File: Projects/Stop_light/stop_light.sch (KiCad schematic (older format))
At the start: 40 parts, among them J1 109159003101916, U1 IS31LT3360, U2 IS31LT3360, U3 IS31LT3360

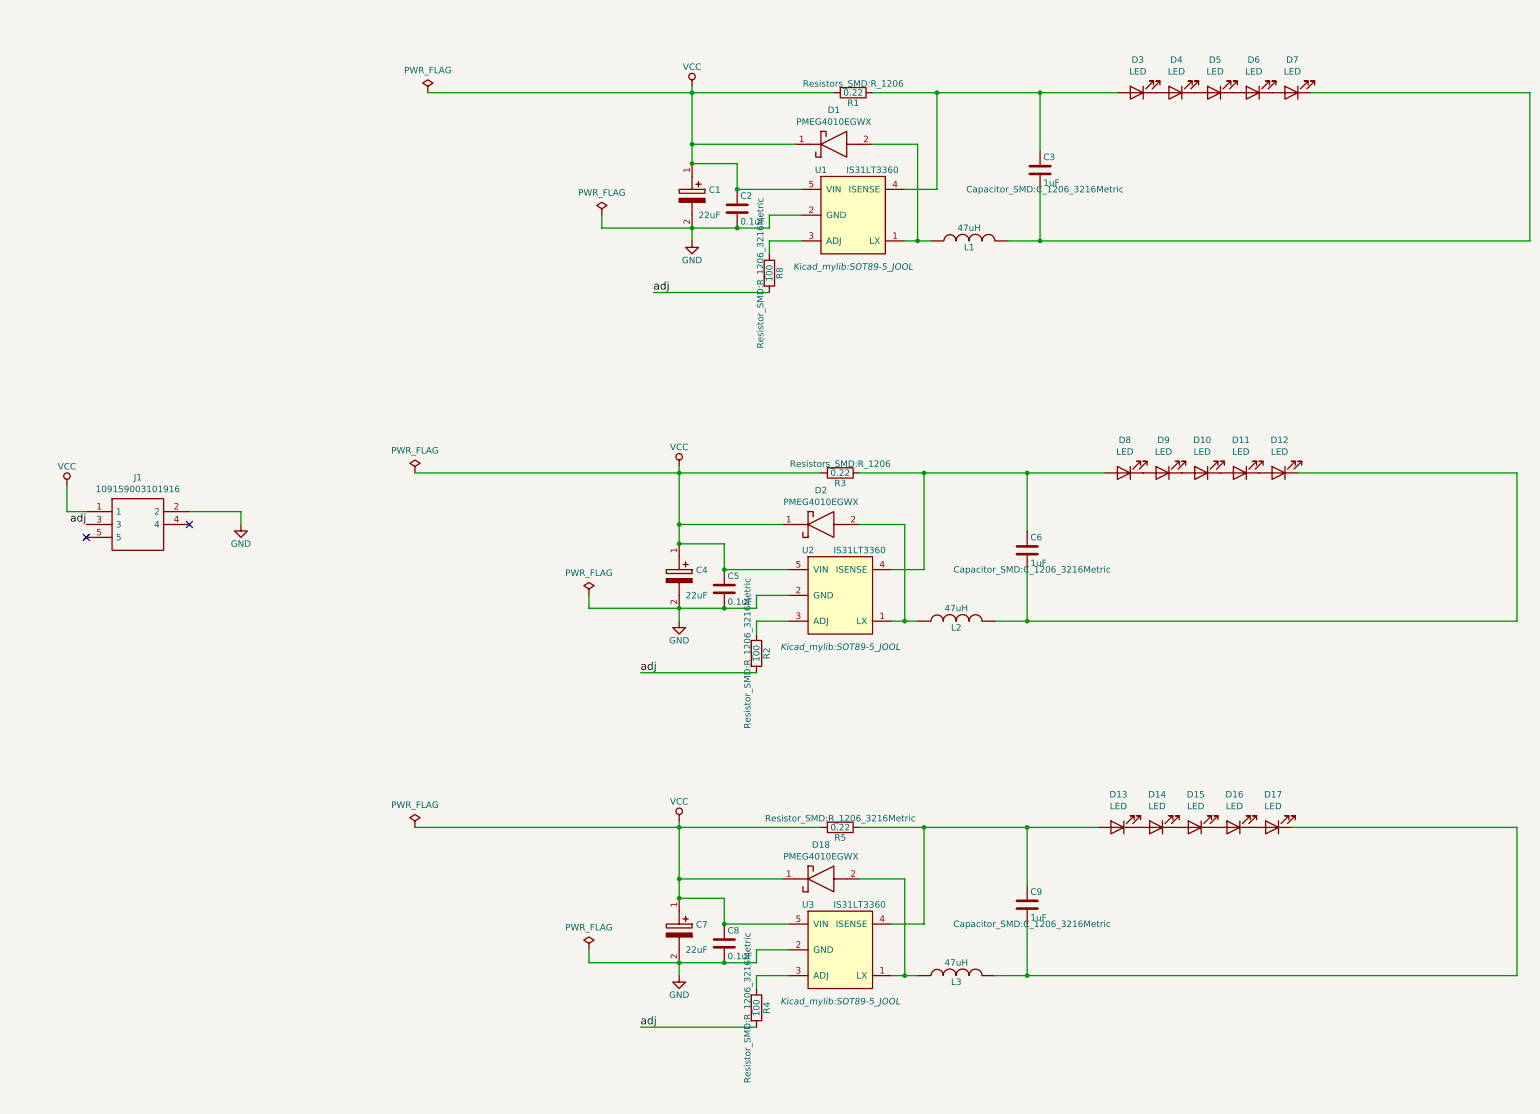
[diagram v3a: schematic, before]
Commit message: stop light updated
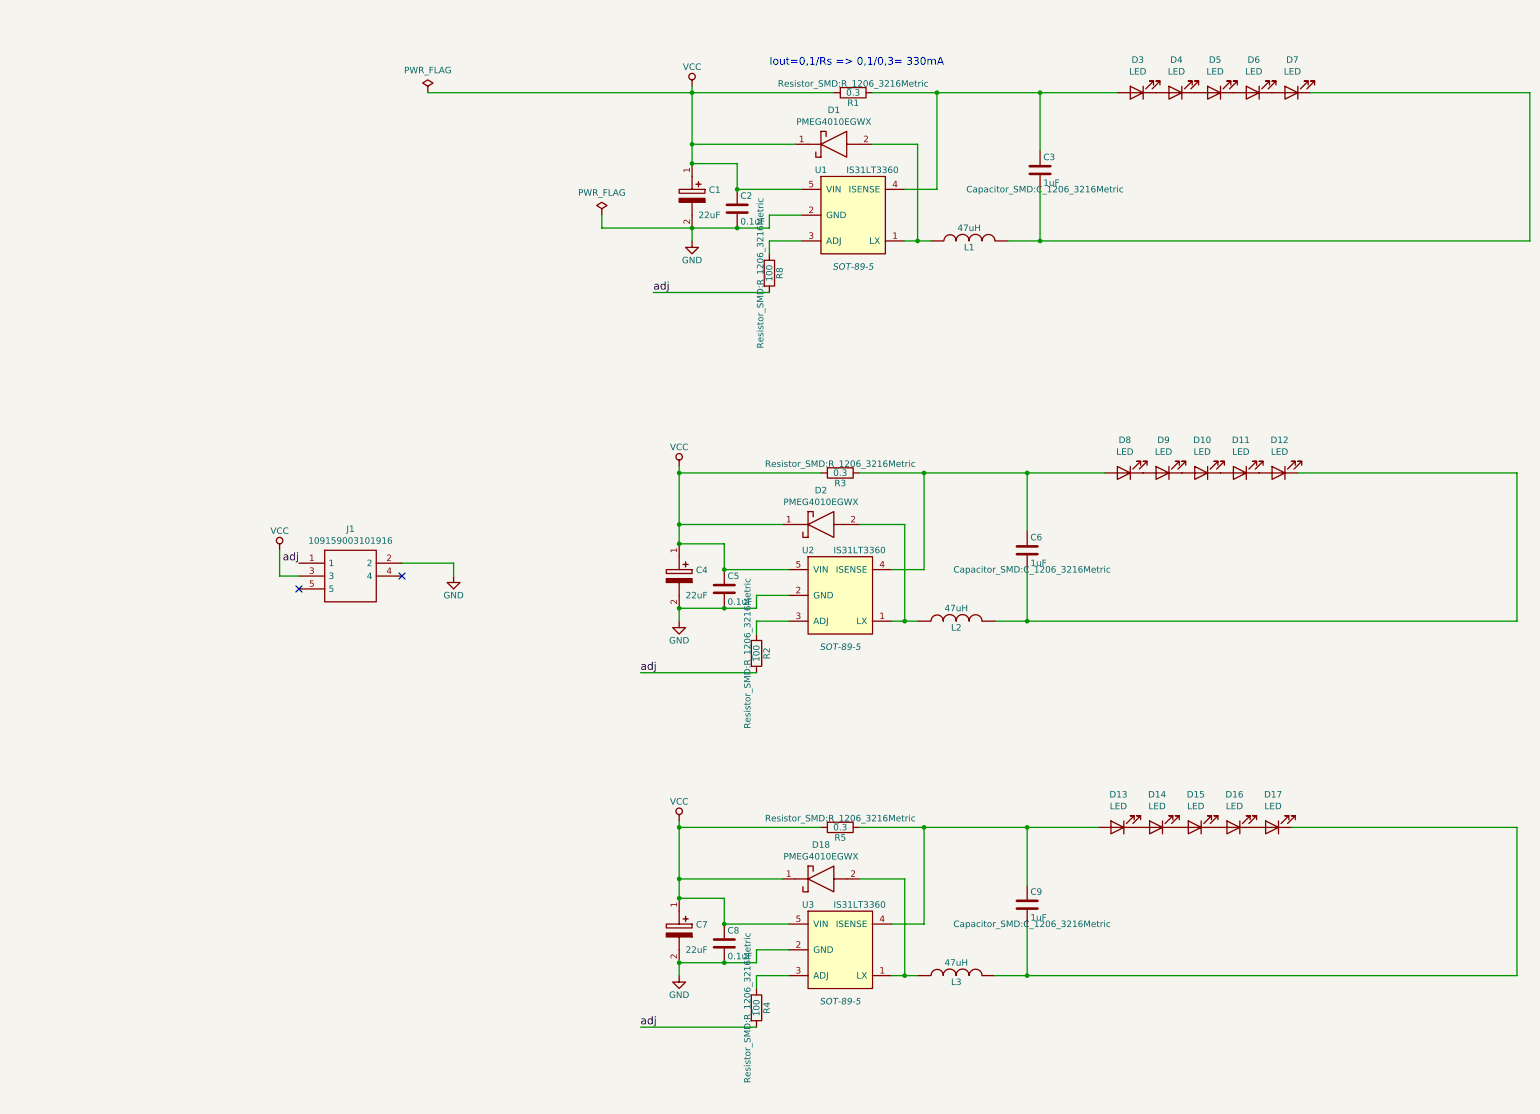
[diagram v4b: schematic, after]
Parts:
- D3: Manufacturer_Part_Number (none) -> DMLQ31.23-HYKY-26-J3T3
- R1, R3: value 0.22 -> 0.3; footprint Resistors_SMD:R_1206 -> Resistor_SMD:R_1206_3216Metric
- R5: value 0.22 -> 0.3
- U1, U2, U3: footprint Kicad_mylib:SOT89-5_JOOL -> SOT-89-5; Manufacturer_Part_Number (none) -> IS31LT3360-SDLS4-TR; Mouser Part Number (none) -> 870-I31LT3360SDLS4TR
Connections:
- net VCC: now also J1.3; no longer J1.1
- net adj: now also J1.1; no longer J1.3
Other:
- note added: "Iout=0,1/Rs => 0,1/0,3= 330mA"
- moved on the sheet: J1
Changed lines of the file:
@@
 F 0 "U1" H 6650 2650 50  0000 C CNN
 F 1 "IS31LT3360" H 7050 2650 50  0000 C CNN
-F 2 "Kicad_mylib:SOT89-5_JOOL" H 6900 1900 50  0000 C CIN
+F 2 "SOT-89-5" H 6900 1900 50  0000 C CIN
 F 3 "www.issi.com/WW/pdf/31LT3360.pdf" H 6950 1800 50  0001 C CNN
+F 4 "IS31LT3360-SDLS4-TR" H 6900 2300 50  0001 C CNN "Manufacturer_Part_Number"
+F 5 "870-I31LT3360SDLS4TR" H 6900 2300 50  0001 C CNN "Mouser Part Number"
 	1    6900 2300
 	1    0    0    -1
@@
 P 6900 1350
 F 0 "R1" V 6980 1350 50  0000 C CNN
-F 1 "0.22" V 6900 1350 50  0000 C CNN
-F 2 "Resistors_SMD:R_1206" V 6830 1350 50  0000 C CNN
+F 1 "0.3" V 6900 1350 50  0000 C CNN
+F 2 "Resistor_SMD:R_1206_3216Metric" V 6830 1350 50  0000 C CNN
 F 3 "" H 6900 1350 50  0000 C CNN
 	1    6900 1350
@@
 F 2 "myKicad_lib:DMLQ31_23" H 9100 1350 50  0001 C CNN
 F 3 "~" H 9100 1350 50  0001 C CNN
+F 4 "DMLQ31.23-HYKY-26-J3T3" H 9100 1350 50  0001 C CNN "Manufacturer_Part_Number"
 	1    9100 1350
 	-1   0    0    1
@@
 F 0 "U2" H 6550 5600 50  0000 C CNN
 F 1 "IS31LT3360" H 6950 5600 50  0000 C CNN
-F 2 "Kicad_mylib:SOT89-5_JOOL" H 6800 4850 50  0000 C CIN
+F 2 "SOT-89-5" H 6800 4850 50  0000 C CIN
 F 3 "www.issi.com/WW/pdf/31LT3360.pdf" H 6850 4750 50  0001 C CNN
+F 4 "IS31LT3360-SDLS4-TR" H 6800 5250 50  0001 C CNN "Manufacturer_Part_Number"
+F 5 "870-I31LT3360SDLS4TR" H 6800 5250 50  0001 C CNN "Mouser Part Number"
 	1    6800 5250
 	1    0    0    -1
@@
 P 6800 4300
 F 0 "R3" V 6880 4300 50  0000 C CNN
-F 1 "0.22" V 6800 4300 50  0000 C CNN
-F 2 "Resistors_SMD:R_1206" V 6730 4300 50  0000 C CNN
+F 1 "0.3" V 6800 4300 50  0000 C CNN
+F 2 "Resistor_SMD:R_1206_3216Metric" V 6730 4300 50  0000 C CNN
 F 3 "" H 6800 4300 50  0000 C CNN
 	1    6800 4300
@@
 Wire Wire Line
 	6150 5450 6400 5450
-Wire Wire Line
-	3500 4300 5550 4300
-$Comp
-L power:PWR_FLAG #FLG01
-U 1 1 5CAFF73F
-P 3500 4300
-F 0 "#FLG01" H 3500 4375 50  0001 C CNN
-F 1 "PWR_FLAG" H 3500 4474 50  0000 C CNN
-F 2 "" H 3500 4300 50  0001 C CNN
-F 3 "~" H 3500 4300 50  0001 C CNN
-	1    3500 4300
-	1    0    0    -1
-$EndComp
 $Comp
 L stop_light-rescue:PMEG4010EGWX-SamacSys_Parts-LED_Driver_ISSI_ALU-rescue D2
@@
 $EndComp
 $Comp
-L power:PWR_FLAG #FLG02
-U 1 1 5CAFF752
-P 4850 5250
-F 0 "#FLG02" H 4850 5325 50  0001 C CNN
-F 1 "PWR_FLAG" H 4850 5424 50  0000 C CNN
-F 2 "" H 4850 5250 50  0001 C CNN
-F 3 "~" H 4850 5250 50  0001 C CNN
-	1    4850 5250
-	1    0    0    -1
-$EndComp
-Wire Wire Line
-	4850 5250 4850 5350
-Wire Wire Line
-	4850 5350 5550 5350
-$Comp
 L stop_light-rescue:R-LED_Driver_ISSI-rescue-LED_Driver_ISSI_ALU-rescue-LED_Driver_ISSI_ALU-rescue-LED_Driver_ISSI_ALU-rescue R2
 U 1 1 5CAFF75D
@@
 F 0 "U3" H 6550 8350 50  0000 C CNN
 F 1 "IS31LT3360" H 6950 8350 50  0000 C CNN
-F 2 "Kicad_mylib:SOT89-5_JOOL" H 6800 7600 50  0000 C CIN
+F 2 "SOT-89-5" H 6800 7600 50  0000 C CIN
 F 3 "www.issi.com/WW/pdf/31LT3360.pdf" H 6850 7500 50  0001 C CNN
+F 4 "IS31LT3360-SDLS4-TR" H 6800 8000 50  0001 C CNN "Manufacturer_Part_Number"
+F 5 "870-I31LT3360SDLS4TR" H 6800 8000 50  0001 C CNN "Mouser Part Number"
 	1    6800 8000
 	1    0    0    -1
@@
 P 6800 7050
 F 0 "R5" V 6880 7050 50  0000 C CNN
-F 1 "0.22" V 6800 7050 50  0000 C CNN
+F 1 "0.3" V 6800 7050 50  0000 C CNN
 F 2 "Resistor_SMD:R_1206_3216Metric" V 6730 7050 50  0000 C CNN
 F 3 "" H 6800 7050 50  0000 C CNN
@@
 Wire Wire Line
 	6150 8200 6400 8200
-Wire Wire Line
-	3500 7050 5550 7050
-$Comp
-L power:PWR_FLAG #FLG03
-U 1 1 5CE915B5
-P 3500 7050
-F 0 "#FLG03" H 3500 7125 50  0001 C CNN
-F 1 "PWR_FLAG" H 3500 7224 50  0000 C CNN
-F 2 "" H 3500 7050 50  0001 C CNN
-F 3 "~" H 3500 7050 50  0001 C CNN
-	1    3500 7050
-	1    0    0    -1
-$EndComp
 $Comp
 L stop_light-rescue:PMEG4010EGWX-SamacSys_Parts-LED_Driver_ISSI_ALU-rescue D18
@@
 $EndComp
 $Comp
-L power:PWR_FLAG #FLG04
-U 1 1 5CE915C7
-P 4850 8000
-F 0 "#FLG04" H 4850 8075 50  0001 C CNN
-F 1 "PWR_FLAG" H 4850 8174 50  0000 C CNN
-F 2 "" H 4850 8000 50  0001 C CNN
-F 3 "~" H 4850 8000 50  0001 C CNN
-	1    4850 8000
-	1    0    0    -1
-$EndComp
-Wire Wire Line
-	4850 8000 4850 8100
-Wire Wire Line
-	4850 8100 5550 8100
-$Comp
 L stop_light-rescue:R-LED_Driver_ISSI-rescue-LED_Driver_ISSI_ALU-rescue-LED_Driver_ISSI_ALU-rescue-LED_Driver_ISSI_ALU-rescue R4
 U 1 1 5CE915D0
@@
 L stop_light-rescue:109159003101916-SamacSys_Parts J1
 U 1 1 5CEDE861
-P 950 4600
-F 0 "J1" H 1350 4865 50  0000 C CNN
-F 1 "109159003101916" H 1350 4774 50  0000 C CNN
-F 2 "SamacSys_Parts:109159003101916" H 1600 4700 50  0001 L CNN
-F 3 "https://componentsearchengine.com/Datasheets/1/109159003101916.pdf" H 1600 4600 50  0001 L CNN
-F 4 "Board to Board & Mezzanine Connectors 3WAY PLUG" H 1600 4500 50  0001 L CNN "Description"
-F 5 "" H 1600 4400 50  0001 L CNN "Height"
-F 6 "581-109159003101916" H 1600 4300 50  0001 L CNN "Mouser Part Number"
-F 7 "https://www.mouser.com/Search/Refine.aspx?Keyword=581-109159003101916" H 1600 4200 50  0001 L CNN "Mouser Price/Stock"
-F 8 "AVX" H 1600 4100 50  0001 L CNN "Manufacturer_Name"
-F 9 "109159003101916" H 1600 4000 50  0001 L CNN "Manufacturer_Part_Number"
-	1    950  4600
-	1    0    0    -1
-$EndComp
-NoConn ~ 950  4800
-NoConn ~ 1750 4700
+P 2600 5000
+F 0 "J1" H 3000 5265 50  0000 C CNN
+F 1 "109159003101916" H 3000 5174 50  0000 C CNN
+F 2 "SamacSys_Parts:109159003101916" H 3250 5100 50  0001 L CNN
+F 3 "https://componentsearchengine.com/Datasheets/1/109159003101916.pdf" H 3250 5000 50  0001 L CNN
+F 4 "Board to Board & Mezzanine Connectors 3WAY PLUG" H 3250 4900 50  0001 L CNN "Description"
+F 5 "" H 3250 4800 50  0001 L CNN "Height"
+F 6 "581-109159003101916" H 3250 4700 50  0001 L CNN "Mouser Part Number"
+F 7 "https://www.mouser.com/Search/Refine.aspx?Keyword=581-109159003101916" H 3250 4600 50  0001 L CNN "Mouser Price/Stock"
+F 8 "AVX" H 3250 4500 50  0001 L CNN "Manufacturer_Name"
+F 9 "109159003101916" H 3250 4400 50  0001 L CNN "Manufacturer_Part_Number"
+	1    2600 5000
+	1    0    0    -1
+$EndComp
+NoConn ~ 2600 5200
+NoConn ~ 3400 5100
 $Comp
 L stop_light-rescue:VCC-LED_Driver_ISSI-rescue-LED_Driver_ISSI_ALU-rescue-LED_Driver_ISSI_ALU-rescue-LED_Driver_ISSI_ALU-rescue #PWR0101
 U 1 1 5CF72751
-P 800 4400
-F 0 "#PWR0101" H 800 4250 50  0001 C CNN
-F 1 "VCC" H 800 4550 50  0000 C CNN
-F 2 "" H 800 4400 50  0000 C CNN
-F 3 "" H 800 4400 50  0000 C CNN
-	1    800  4400
-	1    0    0    -1
-$EndComp
-Wire Wire Line
-	800  4400 800  4600
-Wire Wire Line
-	800  4600 950  4600
+P 2450 4900
+F 0 "#PWR0101" H 2450 4750 50  0001 C CNN
+F 1 "VCC" H 2450 5050 50  0000 C CNN
+F 2 "" H 2450 4900 50  0000 C CNN
+F 3 "" H 2450 4900 50  0000 C CNN
+	1    2450 4900
+	1    0    0    -1
+$EndComp
+Wire Wire Line
+	2450 4900 2450 5100
+Wire Wire Line
+	2450 5100 2600 5100
 $Comp
 L stop_light-rescue:GND-LED_Driver_ISSI-rescue-LED_Driver_ISSI_ALU-rescue-LED_Driver_ISSI_ALU-rescue-LED_Driver_ISSI_ALU-rescue #PWR0102
 U 1 1 5CF769AC
-P 2150 4700
-F 0 "#PWR0102" H 2150 4450 50  0001 C CNN
-F 1 "GND" H 2150 4550 50  0000 C CNN
-F 2 "" H 2150 4700 50  0000 C CNN
-F 3 "" H 2150 4700 50  0000 C CNN
-	1    2150 4700
-	1    0    0    -1
-$EndComp
-Wire Wire Line
-	2150 4700 2150 4600
-Wire Wire Line
-	2150 4600 1750 4600
-Text Label 950  4700 2    60   ~ 0
+P 3800 5100
+F 0 "#PWR0102" H 3800 4850 50  0001 C CNN
+F 1 "GND" H 3800 4950 50  0000 C CNN
+F 2 "" H 3800 5100 50  0000 C CNN
+F 3 "" H 3800 5100 50  0000 C CNN
+	1    3800 5100
+	1    0    0    -1
+$EndComp
+Wire Wire Line
+	3800 5100 3800 5000
+Wire Wire Line
+	3800 5000 3400 5000
+Text Label 2600 5000 2    60   ~ 0
 adj
+Text Notes 6250 1150 0    60   ~ 0
+Iout=0,1/Rs => 0,1/0,3= 330mA
 $EndSCHEMATC
